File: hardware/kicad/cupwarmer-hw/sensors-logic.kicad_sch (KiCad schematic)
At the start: 3 parts, among them J1 I2C Service

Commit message: Update hardware schematics and BOM
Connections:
- net I2C_SCL: now also J1.3 (SCL); no longer J1.2 (GND)
- net I2C_SDA: now also J1.4 (SDA); no longer J1.1 (3V3)
- net SYS_GND: now also J1.2 (GND); no longer J1.3 (SCL)

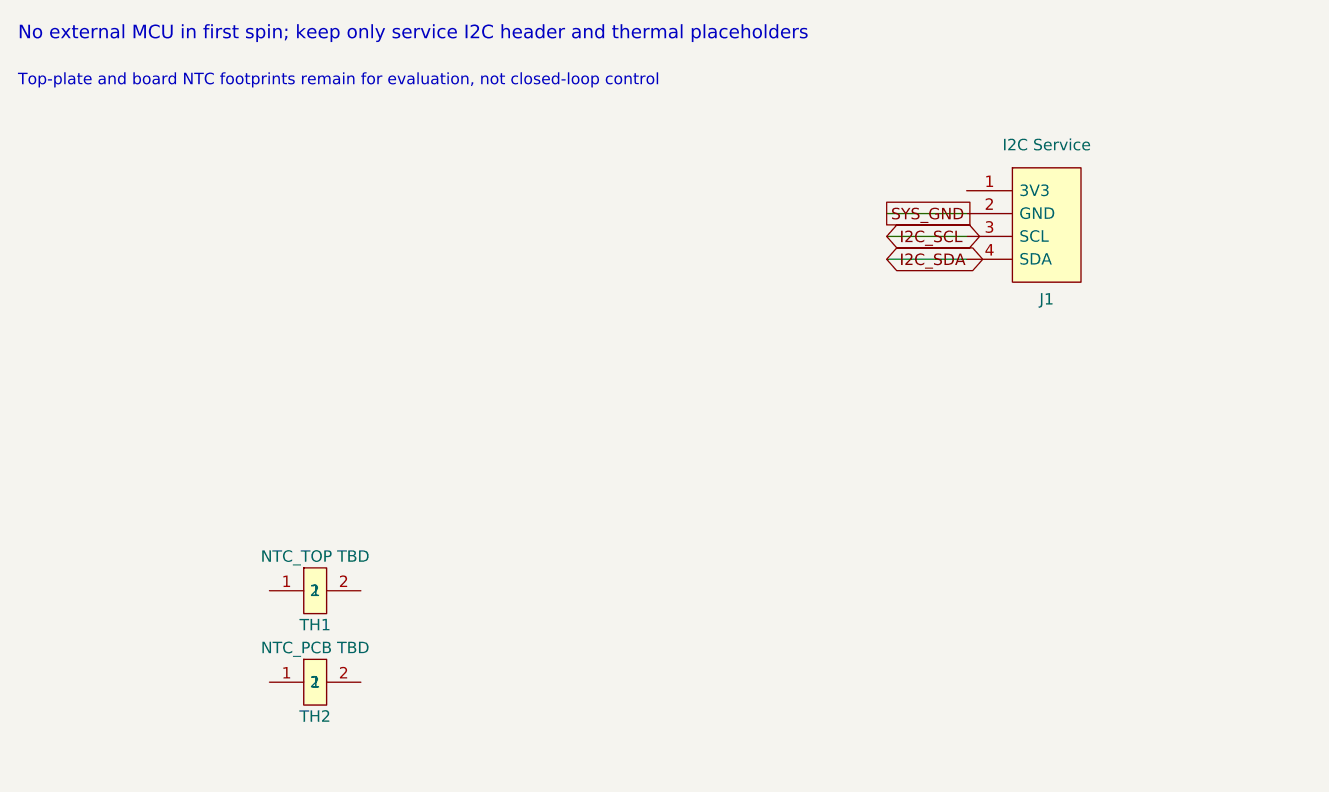
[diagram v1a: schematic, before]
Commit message: Fix KiCad schematic connectivity and symbol sync
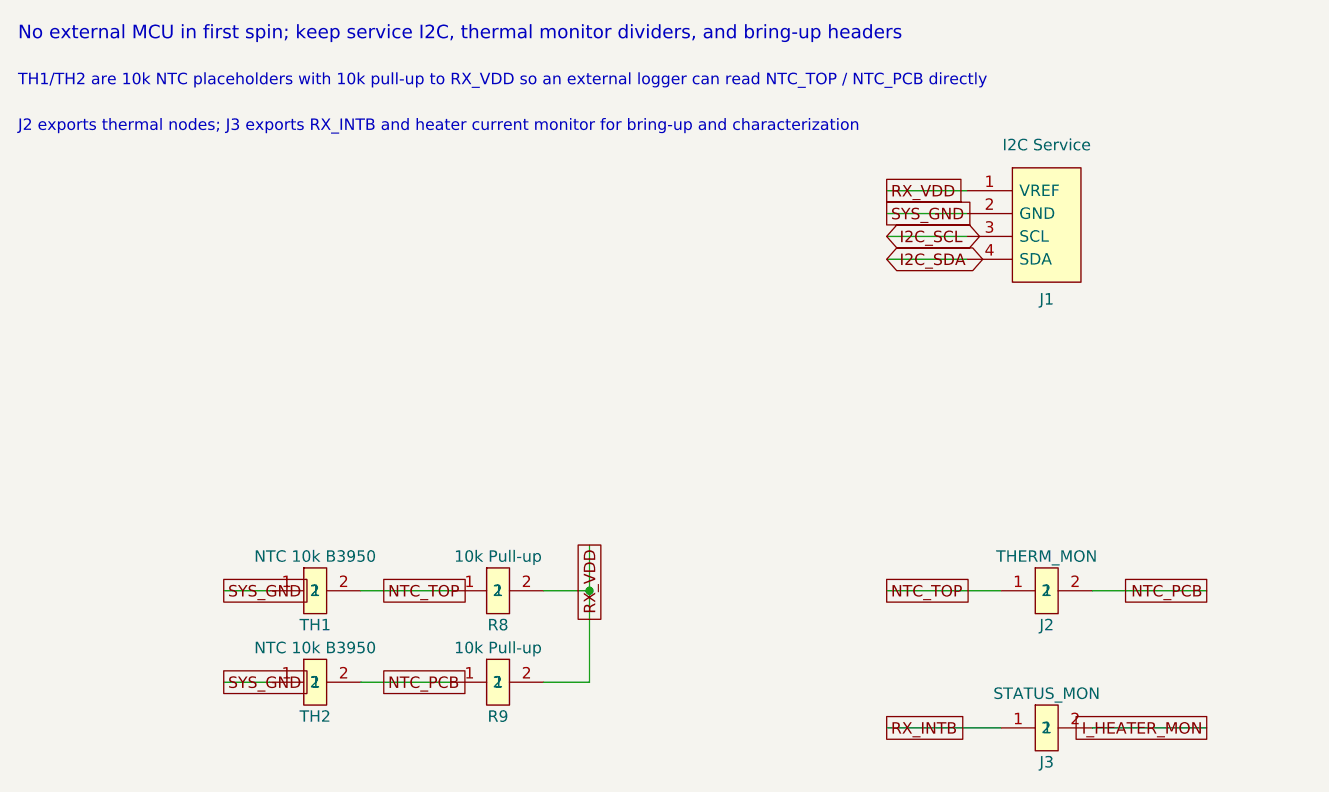
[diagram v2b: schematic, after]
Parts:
- added J2: THERM_MON, symbol cupwarmer:PASSIVE_2
- added J3: STATUS_MON, symbol cupwarmer:PASSIVE_2
- added R8, R9: 10k Pull-up, symbol cupwarmer:PASSIVE_2
- TH1: value NTC_TOP TBD -> NTC 10k B3950
- TH2: value NTC_PCB TBD -> NTC 10k B3950
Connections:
- net SYS_GND: now also TH1.1, TH2.1
- net RX_VDD: now reaches J1.1 (VREF)
- net RX_VDD: now also R8.2, R9.2
- net NTC_TOP: now reaches TH1.2
- net NTC_TOP: now also J2.1, R8.1
- net NTC_PCB: now reaches TH2.2
- net NTC_PCB: now also J2.2, R9.1
- new net I_HEATER_MON: J3.2
- new net RX_INTB: J3.1
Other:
- note added: "J2 exports thermal nodes; J3 exports RX_INTB and heater current monitor for bring-up and characterization"
- note added: "No external MCU in first spin; keep service I2C, thermal monitor dividers, and bring-up headers"
- note added: "TH1/TH2 are 10k NTC placeholders with 10k pull-up to RX_VDD so an external logger can read NTC_TOP / NTC_PCB directly"
- note removed: "No external MCU in first spin; keep only service I2C header and thermal placeholders"
- note removed: "Top-plate and board NTC footprints remain for evaluation, not closed-loop control"
